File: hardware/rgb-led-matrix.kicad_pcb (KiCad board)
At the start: 2 copper layers, 75 x 55 mm, 160 parts, among them J1 AKL_5_2, P1 CONN_01X02, P2 CON-SENSOR, Q1 2N7002P, U1 XMC1XXX24, U2 DRILL, U3 DRILL, U4 DRILL, U5 DRILL

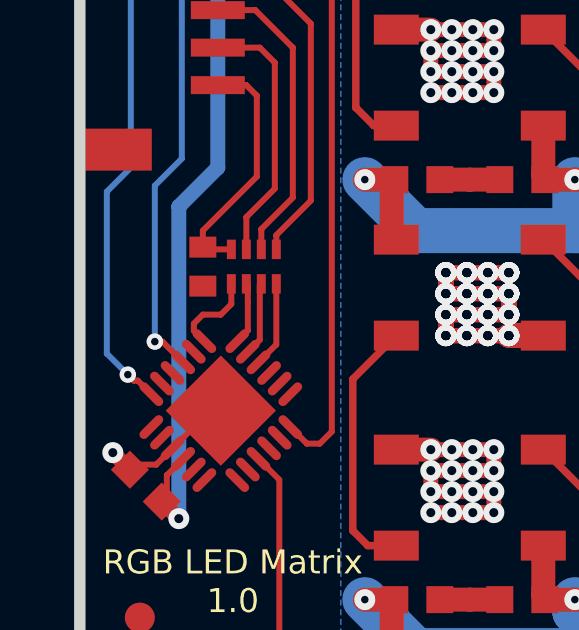
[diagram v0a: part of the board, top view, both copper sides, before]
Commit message: fix led connection
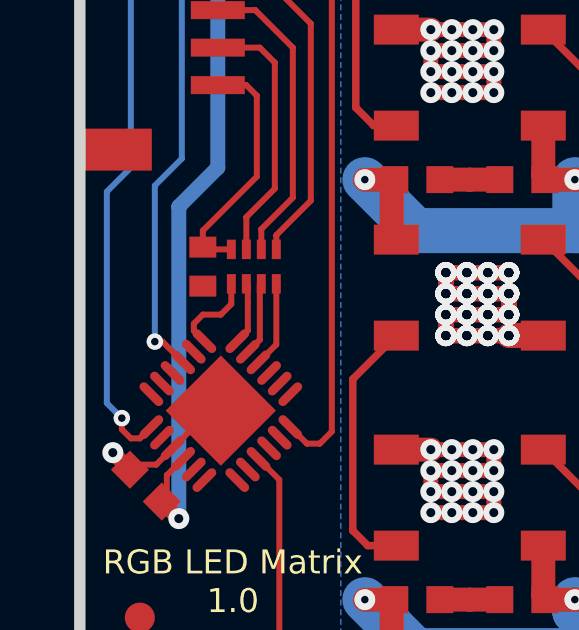
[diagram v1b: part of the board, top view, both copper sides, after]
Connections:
- U1 pad 6: Net-(R1-Pad2) -> (no net)
- U1 pad 7: (no net) -> Net-(R1-Pad2)
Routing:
- net Net-(R1-Pad2): track 24.5 -> 26.5 mm
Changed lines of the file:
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@@
-(kicad_pcb (version 4) (host pcbnew 4.0.2+dfsg1-stable)
+(kicad_pcb (version 4) (host pcbnew 4.0.6-e0-6349~53~ubuntu16.04.1)
   (general
     (links 368)
     (no_connects 0)
-    (area 111.444999 53.444999 282.895869 162.490743)
+    (area 112.109499 54.109499 187.490501 109.490501)
     (thickness 1.6002)
     (drawings 15)
-    (tracks 5643)
+    (tracks 5644)
     (zones 0)
     (modules 160)
@@
   )
   (layers
-    (0 Vorderseite signal hide)
-    (31 Rückseite signal hide)
+    (0 Vorderseite signal)
+    (31 Rückseite signal)
     (32 B.Adhes user)
     (33 F.Adhes user)
@@
     (aux_axis_origin 112.3 54.3)
     (grid_origin 112.3 54.3)
-    (visible_elements FFFFBFFF)
+    (visible_elements FFFF7FFF)
     (pcbplotparams
       (layerselection 0x00030_80000001)
@@
     (pad 4 smd oval (at -2.025 0.25 315) (size 1 0.3) (layers Vorderseite F.Paste F.Mask))
     (pad 5 smd oval (at -2.025 0.75 315) (size 1 0.3) (layers Vorderseite F.Paste F.Mask))
-    (pad 6 smd oval (at -2.025 1.25 315) (size 1 0.3) (layers Vorderseite F.Paste F.Mask)
+    (pad 6 smd oval (at -2.025 1.25 315) (size 1 0.3) (layers Vorderseite F.Paste F.Mask))
+    (pad 7 smd oval (at -1.25 2.025 45) (size 1 0.3) (layers Vorderseite F.Paste F.Mask)
       (net 68 "Net-(R1-Pad2)"))
-    (pad 7 smd oval (at -1.25 2.025 45) (size 1 0.3) (layers Vorderseite F.Paste F.Mask))
     (pad 8 smd oval (at -0.75 2.025 45) (size 1 0.3) (layers Vorderseite F.Paste F.Mask))
     (pad 9 smd oval (at -0.25 2.025 45) (size 1 0.3) (layers Vorderseite F.Paste F.Mask)
@@
   (segment (start 117.6 64.15) (end 117.6 62.727) (width 0.2) (layer Vorderseite) (net 67))
   (segment (start 117.6 62.727) (end 117.611 62.716) (width 0.2) (layer Vorderseite) (net 67))
+  (segment (start 114.684225 96.948008) (end 114.307233 97.325) (width 0.2) (layer Vorderseite) (net 68))
+  (segment (start 113.2 96.15) (end 113.7 96.65) (width 0.2) (layer Rückseite) (net 68))
+  (via (at 113.7 96.65) (size 0.55) (drill 0.25) (layers Vorderseite Rückseite) (net 68))
+  (segment (start 113.2 96.15) (end 113.2 89.1) (width 0.2) (layer Rückseite) (net 68))
+  (segment (start 113.7 97.025) (end 113.7 96.65) (width 0.2) (layer Vorderseite) (net 68))
+  (segment (start 114 97.325) (end 113.7 97.025) (width 0.2) (layer Vorderseite) (net 68))
+  (segment (start 114.307233 97.325) (end 114 97.325) (width 0.2) (layer Vorderseite) (net 68))
   (segment (start 114 72.35) (end 114 73.4) (width 0.2) (layer Vorderseite) (net 68))
-  (segment (start 114.232233 95.4) (end 114.684225 95.851992) (width 0.2) (layer Vorderseite) (net 68))
-  (segment (start 114.1 95.4) (end 114.232233 95.4) (width 0.2) (layer Vorderseite) (net 68))
-  (segment (start 113.9 95.2) (end 114.1 95.4) (width 0.2) (layer Vorderseite) (net 68))
-  (via (at 113.9 95.2) (size 0.55) (drill 0.25) (layers Vorderseite Rückseite) (net 68))
-  (segment (start 113.2 94.5) (end 113.9 95.2) (width 0.2) (layer Rückseite) (net 68))
-  (segment (start 113.2 89.1) (end 113.2 94.5) (width 0.2) (layer Rückseite) (net 68))
   (segment (start 114 88.3) (end 113.2 89.1) (width 0.2) (layer Rückseite) (net 68))
   (segment (start 114 73.4) (end 114 88.3) (width 0.2) (layer Rückseite) (net 68))

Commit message: define ferrite
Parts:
- FB2: value FILTER -> FB 6A
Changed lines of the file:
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@@
     (links 368)
     (no_connects 0)
-    (area 112.109499 54.109499 187.490501 109.490501)
+    (area 111.444999 53.444999 282.795857 162.890793)
     (thickness 1.6002)
     (drawings 15)
@@
   )
   (layers
-    (0 Vorderseite signal)
-    (31 Rückseite signal)
+    (0 Vorderseite signal hide)
+    (31 Rückseite signal hide)
     (32 B.Adhes user)
     (33 F.Adhes user)
@@
       (effects (font (size 0.3 0.3) (thickness 0.075)))
     )
-    (fp_text value FILTER (at 0 -0.65 270) (layer F.Fab)
+    (fp_text value "FB 6A" (at 0 -0.65 270) (layer F.Fab)
       (effects (font (size 0.3 0.3) (thickness 0.075)))
     )

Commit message: Add 3d information (fam)
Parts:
- RP1: footprint 4X0402 -> kicad-libraries:4X0402

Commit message: specify filter circuit
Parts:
- C70: value TBD -> 220pF
- RP1: value TBD -> 82
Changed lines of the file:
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@@
-(kicad_pcb (version 4) (host pcbnew 4.0.2+dfsg1-stable)
+(kicad_pcb (version 4) (host pcbnew 4.0.7-e0-6372~58~ubuntu16.10.1)
   (general
     (links 368)
@@
       (effects (font (size 0.2 0.2) (thickness 0.05)))
     )
-    (fp_text value TBD (at 0 -0.275 90) (layer F.Fab)
+    (fp_text value 220pF (at 0 -0.275 90) (layer F.Fab)
       (effects (font (size 0.2 0.2) (thickness 0.05)))
     )
@@
       (effects (font (size 0.2 0.2) (thickness 0.05)))
     )
-    (fp_text value TBD (at -0.025 -0.45 180) (layer F.Fab)
+    (fp_text value 82 (at -0.025 -0.45 180) (layer F.Fab)
       (effects (font (size 0.2 0.2) (thickness 0.05)))
     )

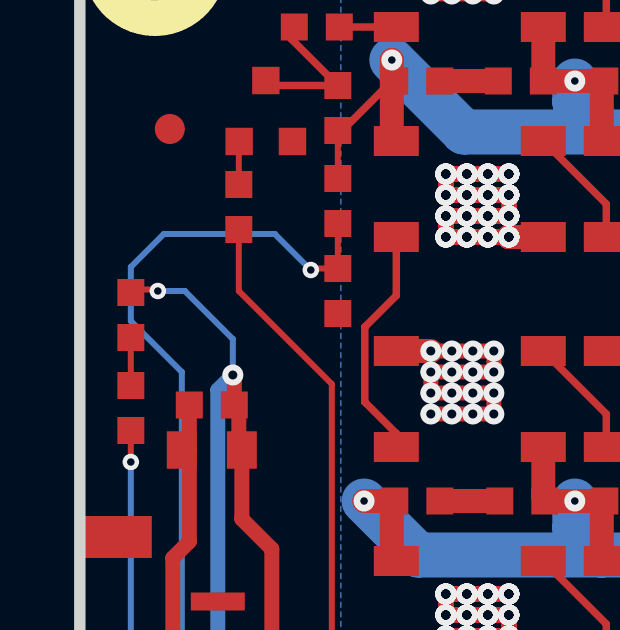
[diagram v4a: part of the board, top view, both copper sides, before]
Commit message: add status led description text
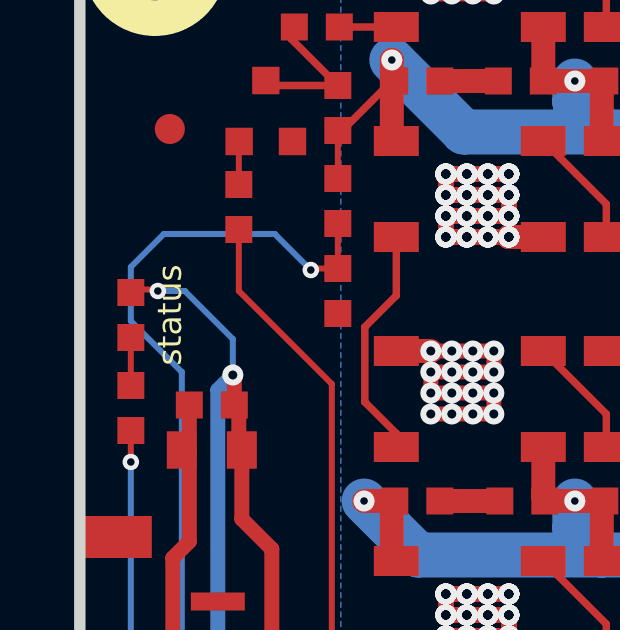
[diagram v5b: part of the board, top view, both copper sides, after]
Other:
- board text added: "status"
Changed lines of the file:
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@@
-(kicad_pcb (version 4) (host pcbnew 4.0.7-e0-6372~58~ubuntu16.10.1)
+(kicad_pcb (version 4) (host pcbnew 4.0.7-e2-6376~58~ubuntu17.04.1)
   (general
     (links 368)
     (no_connects 0)
-    (area 112.109499 54.109499 187.490501 109.490501)
+    (area 111.444999 53.444999 282.795857 162.890793)
     (thickness 1.6002)
-    (drawings 15)
+    (drawings 16)
     (tracks 5644)
     (zones 0)
@@
     )
   )
+  (gr_text status (at 115.3 68.5 90) (layer F.SilkS)
+    (effects (font (size 0.8001 0.8001) (thickness 0.14986)))
+  )
   (gr_text 5V (at 186.5 84.3 90) (layer B.SilkS)

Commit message: specify processor
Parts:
- U1: value XMC1XXX24 -> XMC1100-16
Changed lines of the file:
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@@
       (effects (font (size 0.3 0.3) (thickness 0.075)))
     )
-    (fp_text value XMC1XXX24 (at 0 0.8 315) (layer F.Fab)
+    (fp_text value XMC1100-16 (at 0 0.8 315) (layer F.Fab)
       (effects (font (size 0.3 0.3) (thickness 0.075)))
     )
